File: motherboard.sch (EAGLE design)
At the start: 132 parts, among them IC1 LM2576, IC10 TUSB2046B, IC11 OPA129U, IC2 74LS595D, IC3 74LS595D, IC4 IC_FT230X-SSOP-16, IC5 VN5772AK, IC6 VN5772AK, IC7 VN5772AK, IC8 VN5772AK, IC9 VN5772AK, U2 V_REG_LDOSMD, U3 ATMEGA168, Y1 16Mhz, Y2 6MHz

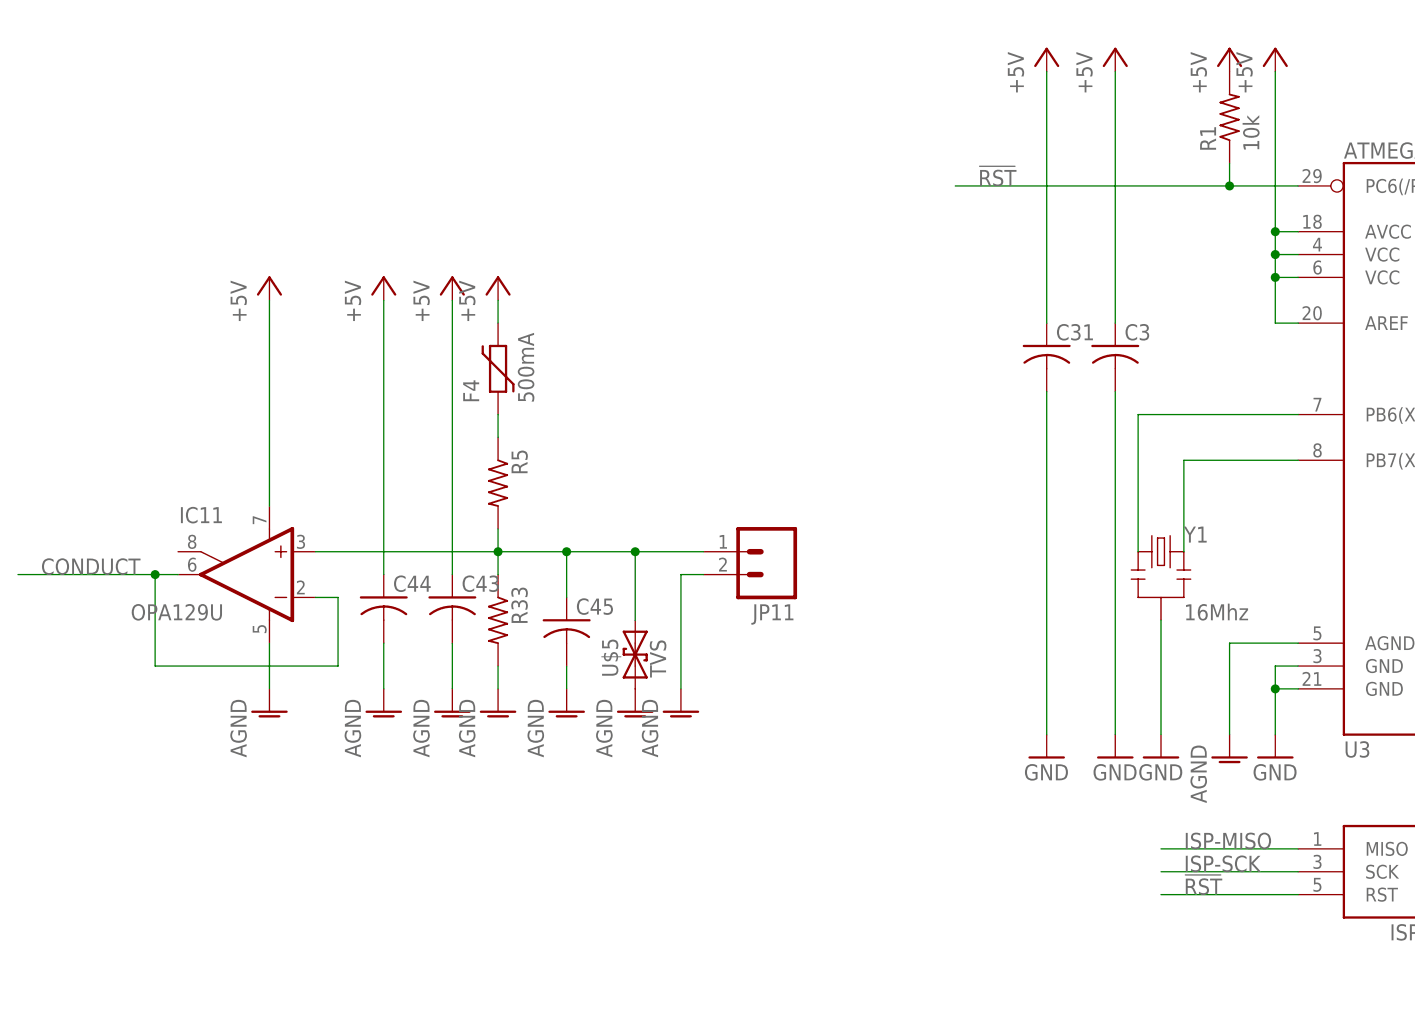
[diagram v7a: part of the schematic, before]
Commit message: reorganized analog sensor
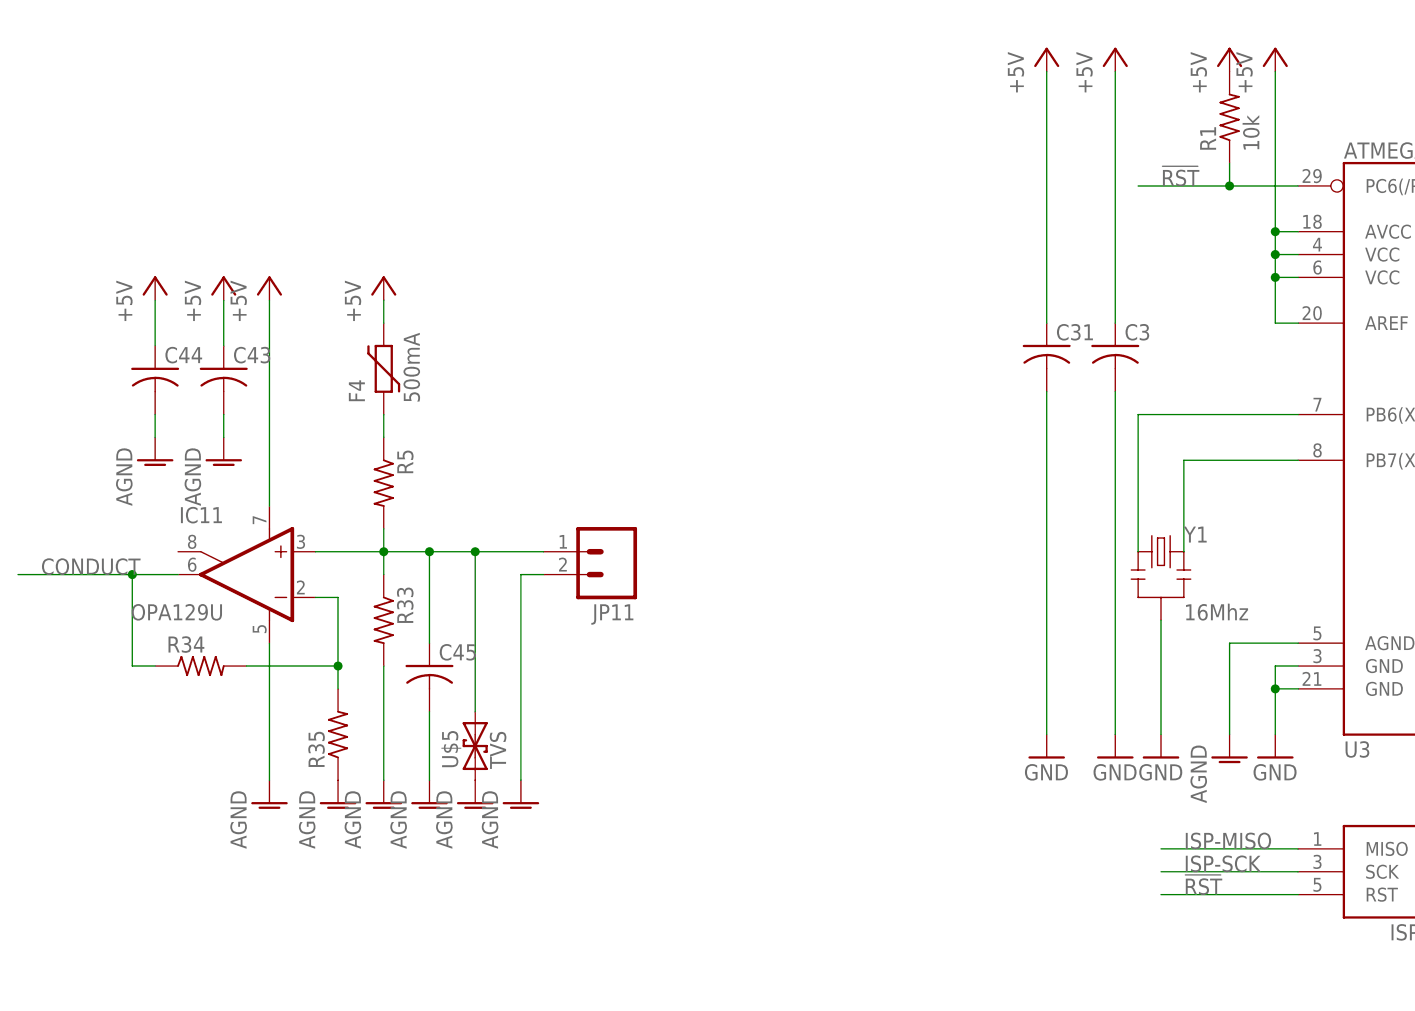
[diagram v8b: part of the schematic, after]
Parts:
- added R34, R35: (no value), adafruit:R-US_R1206
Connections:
- new net N$54: IC11.-IN, R34.2, R35.2
- net AGND: now also R35.1
- net CONDUCT: now also R34.1; no longer IC11.-IN
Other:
- moved on the sheet: C43, C44, C45, F4, JP11, R33, R5, U$5
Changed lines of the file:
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@@
 <part name="C45" library="adafruit" deviceset="C-US" device="C1206"/>
 <part name="AGND8" library="supply1" deviceset="AGND" device=""/>
+<part name="R34" library="adafruit" deviceset="R-US_" device="R1206"/>
+<part name="R35" library="adafruit" deviceset="R-US_" device="R1206"/>
+<part name="AGND9" library="supply1" deviceset="AGND" device=""/>
 </parts>
 <sheets>
@@
 <instance part="C42" gate="G$1" x="269.24" y="27.94" rot="MR0"/>
 <instance part="GND86" gate="1" x="269.24" y="15.24"/>
-<instance part="R5" gate="G$1" x="12.7" y="233.68" rot="R270"/>
-<instance part="R33" gate="G$1" x="12.7" y="218.44" rot="R270"/>
-<instance part="P+36" gate="1" x="12.7" y="256.54"/>
-<instance part="F4" gate="G$1" x="12.7" y="246.38" rot="R90"/>
-<instance part="AGND2" gate="VR1" x="12.7" y="208.28"/>
+<instance part="R5" gate="G$1" x="0" y="233.68" rot="R270"/>
+<instance part="R33" gate="G$1" x="0" y="218.44" rot="R270"/>
+<instance part="P+36" gate="1" x="0" y="256.54"/>
+<instance part="F4" gate="G$1" x="0" y="246.38" rot="R90"/>
+<instance part="AGND2" gate="VR1" x="0" y="198.12"/>
 <instance part="IC11" gate="G$1" x="-15.24" y="223.52" rot="MR0"/>
 <instance part="P+37" gate="1" x="-12.7" y="256.54"/>
-<instance part="AGND3" gate="VR1" x="-12.7" y="208.28"/>
-<instance part="U$5" gate="G$1" x="27.94" y="213.36" rot="R90"/>
-<instance part="AGND4" gate="VR1" x="27.94" y="208.28"/>
-<instance part="JP11" gate="G$1" x="43.18" y="226.06" rot="R180"/>
-<instance part="AGND5" gate="VR1" x="33.02" y="208.28"/>
-<instance part="C43" gate="G$1" x="7.62" y="220.98"/>
-<instance part="C44" gate="G$1" x="0" y="220.98"/>
-<instance part="AGND6" gate="VR1" x="7.62" y="208.28"/>
-<instance part="AGND7" gate="VR1" x="0" y="208.28"/>
-<instance part="P+38" gate="1" x="0" y="256.54"/>
-<instance part="P+39" gate="1" x="7.62" y="256.54"/>
-<instance part="C45" gate="G$1" x="20.32" y="218.44"/>
-<instance part="AGND8" gate="VR1" x="20.32" y="208.28"/>
+<instance part="AGND3" gate="VR1" x="-12.7" y="198.12"/>
+<instance part="U$5" gate="G$1" x="10.16" y="203.2" rot="R90"/>
+<instance part="AGND4" gate="VR1" x="10.16" y="198.12"/>
+<instance part="JP11" gate="G$1" x="25.4" y="226.06" rot="R180"/>
+<instance part="AGND5" gate="VR1" x="15.24" y="198.12"/>
+<instance part="C43" gate="G$1" x="-17.78" y="246.38"/>
+<instance part="C44" gate="G$1" x="-25.4" y="246.38"/>
+<instance part="AGND6" gate="VR1" x="-17.78" y="236.22"/>
+<instance part="AGND7" gate="VR1" x="-25.4" y="236.22"/>
+<instance part="P+38" gate="1" x="-25.4" y="256.54"/>
+<instance part="P+39" gate="1" x="-17.78" y="256.54"/>
+<instance part="C45" gate="G$1" x="5.08" y="213.36"/>
+<instance part="AGND8" gate="VR1" x="5.08" y="198.12"/>
+<instance part="R34" gate="G$1" x="-20.32" y="213.36"/>
+<instance part="R35" gate="G$1" x="-5.08" y="205.74" rot="R90"/>
+<instance part="AGND9" gate="VR1" x="-5.08" y="198.12"/>
 </instances>
 <busses>
@@
 <pinref part="F4" gate="G$1" pin="2"/>
 <pinref part="P+36" gate="1" pin="+5V"/>
-<wire x1="12.7" y1="251.46" x2="12.7" y2="254" width="0.1524" layer="91"/>
+<wire x1="0" y1="251.46" x2="0" y2="254" width="0.1524" layer="91"/>
 </segment>
 <segment>
@@
 <pinref part="C44" gate="G$1" pin="1"/>
 <pinref part="P+38" gate="1" pin="+5V"/>
-<wire x1="0" y1="254" x2="0" y2="223.52" width="0.1524" layer="91"/>
+<wire x1="-25.4" y1="254" x2="-25.4" y2="248.92" width="0.1524" layer="91"/>
 </segment>
 <segment>
 <pinref part="C43" gate="G$1" pin="1"/>
 <pinref part="P+39" gate="1" pin="+5V"/>
-<wire x1="7.62" y1="254" x2="7.62" y2="223.52" width="0.1524" layer="91"/>
+<wire x1="-17.78" y1="254" x2="-17.78" y2="248.92" width="0.1524" layer="91"/>
 </segment>
 </net>
@@
 <wire x1="101.6" y1="266.7" x2="93.98" y2="266.7" width="0.1524" layer="91"/>
 <wire x1="93.98" y1="266.7" x2="93.98" y2="269.24" width="0.1524" layer="91"/>
-<wire x1="93.98" y1="266.7" x2="63.5" y2="266.7" width="0.1524" layer="91"/>
+<wire x1="93.98" y1="266.7" x2="83.82" y2="266.7" width="0.1524" layer="91"/>
 <junction x="93.98" y="266.7"/>
-<label x="66.04" y="266.7" size="1.778" layer="95"/>
+<label x="86.36" y="266.7" size="1.778" layer="95"/>
 <pinref part="U3" gate="G$1" pin="PC6(/RESET)"/>
 </segment>
@@
 <pinref part="R33" gate="G$1" pin="2"/>
 <pinref part="AGND2" gate="VR1" pin="AGND"/>
-<wire x1="12.7" y1="210.82" x2="12.7" y2="213.36" width="0.1524" layer="91"/>
+<wire x1="0" y1="200.66" x2="0" y2="213.36" width="0.1524" layer="91"/>
 </segment>
 <segment>
 <pinref part="IC11" gate="G$1" pin="V-"/>
 <pinref part="AGND3" gate="VR1" pin="AGND"/>
-<wire x1="-12.7" y1="210.82" x2="-12.7" y2="215.9" width="0.1524" layer="91"/>
+<wire x1="-12.7" y1="200.66" x2="-12.7" y2="215.9" width="0.1524" layer="91"/>
 </segment>
 <segment>
@@
 <pinref part="JP11" gate="G$1" pin="2"/>
 <pinref part="AGND5" gate="VR1" pin="AGND"/>
-<wire x1="33.02" y1="210.82" x2="33.02" y2="223.52" width="0.1524" layer="91"/>
-<wire x1="33.02" y1="223.52" x2="35.56" y2="223.52" width="0.1524" layer="91"/>
+<wire x1="15.24" y1="200.66" x2="15.24" y2="223.52" width="0.1524" layer="91"/>
+<wire x1="15.24" y1="223.52" x2="17.78" y2="223.52" width="0.1524" layer="91"/>
 </segment>
 <segment>
 <pinref part="AGND7" gate="VR1" pin="AGND"/>
 <pinref part="C44" gate="G$1" pin="2"/>
-<wire x1="0" y1="215.9" x2="0" y2="210.82" width="0.1524" layer="91"/>
+<wire x1="-25.4" y1="241.3" x2="-25.4" y2="238.76" width="0.1524" layer="91"/>
 </segment>
 <segment>
 <pinref part="AGND6" gate="VR1" pin="AGND"/>
 <pinref part="C43" gate="G$1" pin="2"/>
-<wire x1="7.62" y1="215.9" x2="7.62" y2="210.82" width="0.1524" layer="91"/>
+<wire x1="-17.78" y1="241.3" x2="-17.78" y2="238.76" width="0.1524" layer="91"/>
 </segment>
 <segment>
 <pinref part="C45" gate="G$1" pin="2"/>
 <pinref part="AGND8" gate="VR1" pin="AGND"/>
-<wire x1="20.32" y1="210.82" x2="20.32" y2="213.36" width="0.1524" layer="91"/>
+<wire x1="5.08" y1="200.66" x2="5.08" y2="208.28" width="0.1524" layer="91"/>
+</segment>
+<segment>
+<pinref part="R35" gate="G$1" pin="1"/>
+<pinref part="AGND9" gate="VR1" pin="AGND"/>
 </segment>
 </net>
@@
 </segment>
 <segment>
-<pinref part="IC11" gate="G$1" pin="-IN"/>
-<wire x1="-7.62" y1="220.98" x2="-5.08" y2="220.98" width="0.1524" layer="91"/>
-<wire x1="-5.08" y1="220.98" x2="-5.08" y2="213.36" width="0.1524" layer="91"/>
-<wire x1="-5.08" y1="213.36" x2="-25.4" y2="213.36" width="0.1524" layer="91"/>
-<wire x1="-25.4" y1="213.36" x2="-25.4" y2="223.52" width="0.1524" layer="91"/>
 <pinref part="IC11" gate="G$1" pin="OUT"/>
-<wire x1="-25.4" y1="223.52" x2="-22.86" y2="223.52" width="0.1524" layer="91"/>
-<wire x1="-25.4" y1="223.52" x2="-40.64" y2="223.52" width="0.1524" layer="91"/>
-<junction x="-25.4" y="223.52"/>
+<wire x1="-22.86" y1="223.52" x2="-27.94" y2="223.52" width="0.1524" layer="91"/>
 <label x="-38.1" y="223.52" size="1.778" layer="95"/>
+<pinref part="R34" gate="G$1" pin="1"/>
+<wire x1="-27.94" y1="223.52" x2="-40.64" y2="223.52" width="0.1524" layer="91"/>
+<wire x1="-25.4" y1="213.36" x2="-27.94" y2="213.36" width="0.1524" layer="91"/>
+<wire x1="-27.94" y1="213.36" x2="-27.94" y2="223.52" width="0.1524" layer="91"/>
+<junction x="-27.94" y="223.52"/>
 </segment>
 </net>
@@
 <pinref part="R5" gate="G$1" pin="1"/>
 <pinref part="F4" gate="G$1" pin="1"/>
-<wire x1="12.7" y1="241.3" x2="12.7" y2="238.76" width="0.1524" layer="91"/>
+<wire x1="0" y1="241.3" x2="0" y2="238.76" width="0.1524" layer="91"/>
 </segment>
 </net>
@@
 <pinref part="R5" gate="G$1" pin="2"/>
 <pinref part="R33" gate="G$1" pin="1"/>
-<wire x1="12.7" y1="223.52" x2="12.7" y2="226.06" width="0.1524" layer="91"/>
+<wire x1="0" y1="223.52" x2="0" y2="226.06" width="0.1524" layer="91"/>
 <pinref part="IC11" gate="G$1" pin="+IN"/>
-<wire x1="12.7" y1="226.06" x2="12.7" y2="228.6" width="0.1524" layer="91"/>
-<wire x1="-7.62" y1="226.06" x2="12.7" y2="226.06" width="0.1524" layer="91"/>
-<junction x="12.7" y="226.06"/>
-<wire x1="12.7" y1="226.06" x2="20.32" y2="226.06" width="0.1524" layer="91"/>
+<wire x1="0" y1="226.06" x2="0" y2="228.6" width="0.1524" layer="91"/>
+<wire x1="-7.62" y1="226.06" x2="0" y2="226.06" width="0.1524" layer="91"/>
+<junction x="0" y="226.06"/>
+<wire x1="0" y1="226.06" x2="5.08" y2="226.06" width="0.1524" layer="91"/>
 <pinref part="U$5" gate="G$1" pin="2"/>
-<wire x1="20.32" y1="226.06" x2="27.94" y2="226.06" width="0.1524" layer="91"/>
-<wire x1="27.94" y1="226.06" x2="27.94" y2="218.44" width="0.1524" layer="91"/>
+<wire x1="5.08" y1="226.06" x2="10.16" y2="226.06" width="0.1524" layer="91"/>
+<wire x1="10.16" y1="226.06" x2="10.16" y2="208.28" width="0.1524" layer="91"/>
 <pinref part="JP11" gate="G$1" pin="1"/>
-<wire x1="27.94" y1="226.06" x2="35.56" y2="226.06" width="0.1524" layer="91"/>
-<junction x="27.94" y="226.06"/>
+<wire x1="10.16" y1="226.06" x2="17.78" y2="226.06" width="0.1524" layer="91"/>
+<junction x="10.16" y="226.06"/>
 <pinref part="C45" gate="G$1" pin="1"/>
-<wire x1="20.32" y1="220.98" x2="20.32" y2="226.06" width="0.1524" layer="91"/>
-<junction x="20.32" y="226.06"/>
-</segment>
-</net>
+<wire x1="5.08" y1="215.9" x2="5.08" y2="226.06" width="0.1524" layer="91"/>
+<junction x="5.08" y="226.06"/>
+</segment>
+</net>
+<net name="N$54" class="0">
+<segment>
+<pinref part="IC11" gate="G$1" pin="-IN"/>
+<wire x1="-7.62" y1="220.98" x2="-5.08" y2="220.98" width="0.1524" layer="91"/>
+<wire x1="-5.08" y1="220.98" x2="-5.08" y2="213.36" width="0.1524" layer="91"/>
+<wire x1="-5.08" y1="213.36" x2="-15.24" y2="213.36" width="0.1524" layer="91"/>
+<pinref part="R34" gate="G$1" pin="2"/>
+<junction x="-5.08" y="213.36"/>
+<pinref part="R35" gate="G$1" pin="2"/>
+<wire x1="-5.08" y1="210.82" x2="-5.08" y2="213.36" width="0.1524" layer="91"/>
+</segment>
+</net>
